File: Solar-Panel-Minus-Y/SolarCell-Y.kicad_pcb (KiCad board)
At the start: 6 copper layers, 64 x 58 mm, 61 parts, among them IC2 TSL2561, J1 XF2M-1015-1A, J3 BATTERY CONNECTOR, J4 B2B-PH-SM4-TB_LF__SN_, U2 Value, U3 SW_SPDT, U4 SW_SPDT

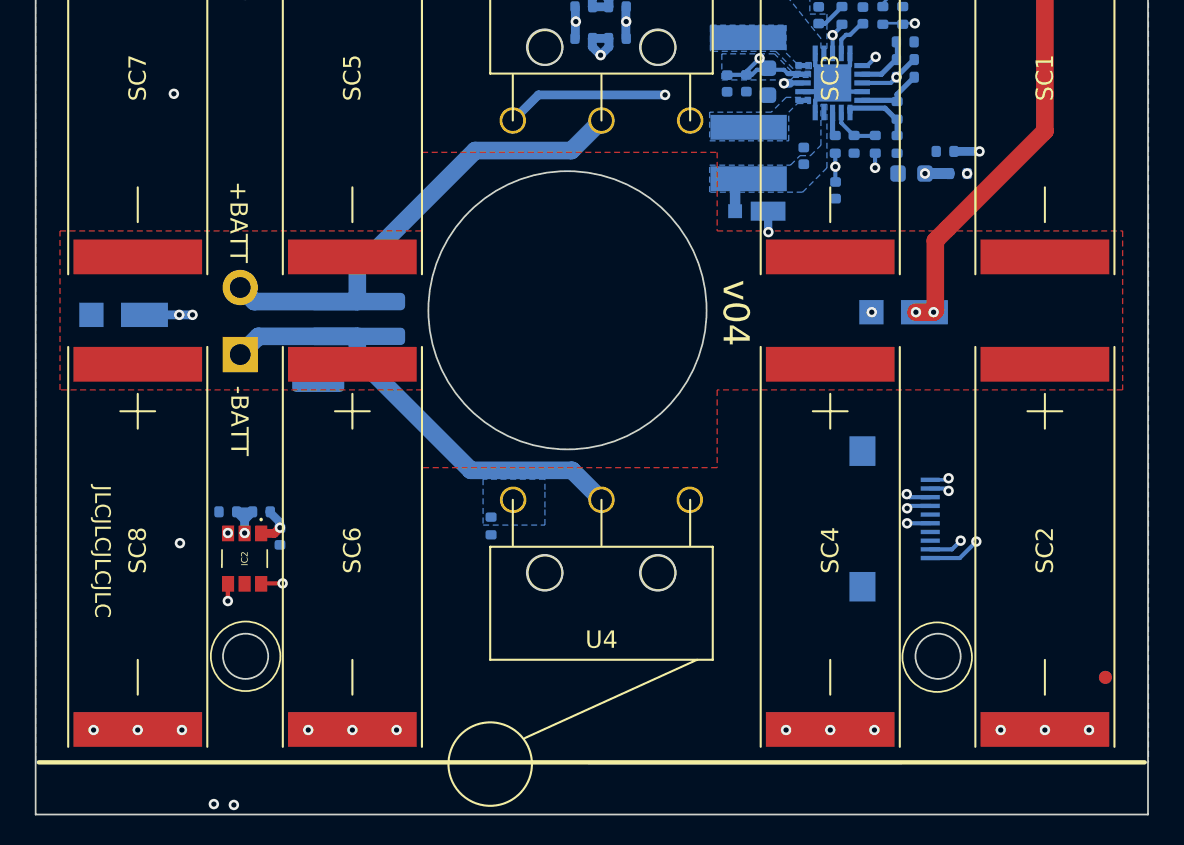
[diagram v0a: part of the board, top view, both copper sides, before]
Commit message: Added missing caps and fixed manufacturing error
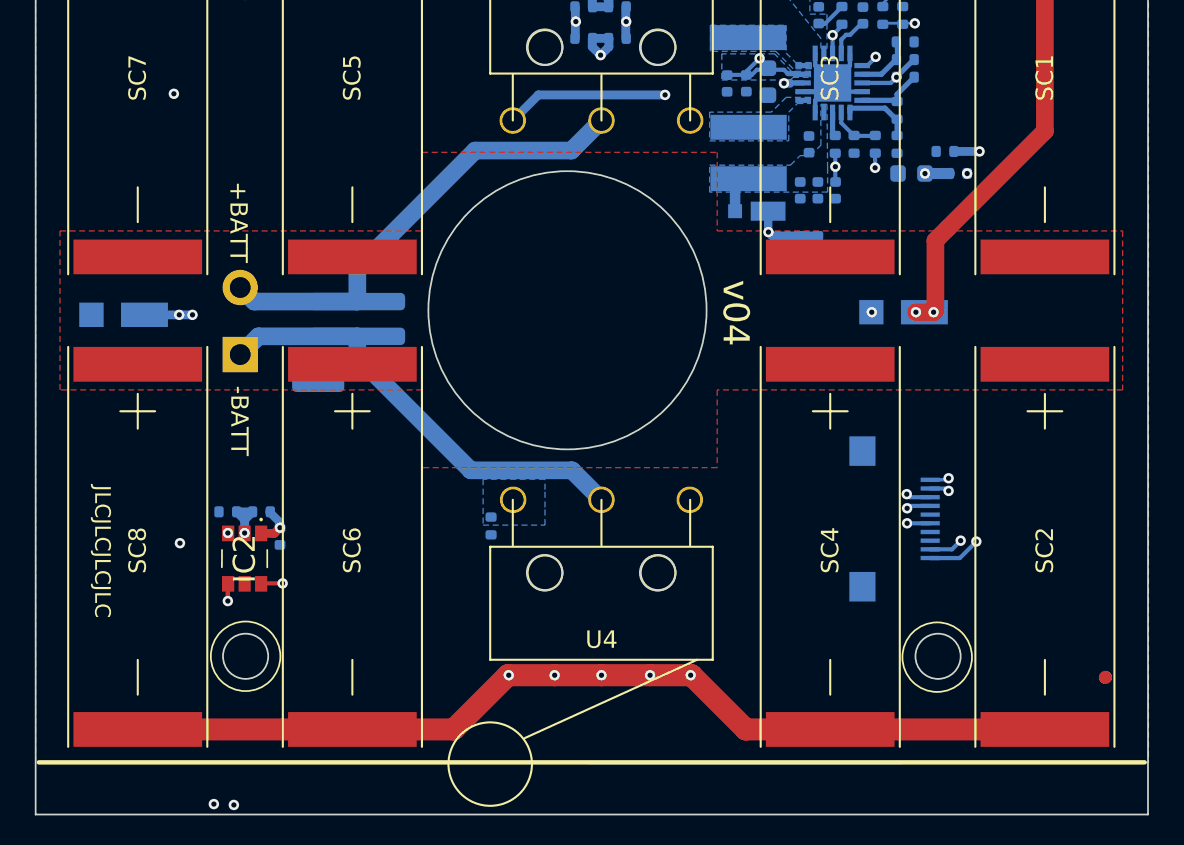
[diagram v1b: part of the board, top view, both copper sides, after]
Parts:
- added C11: 0.1uF, Capacitor_SMD:C_0402_1005Metric, B.Cu at (158.0, 92.1)
- added C12: 100uF, Capacitor_SMD:C_0402_1005Metric, B.Cu at (157.0, 92.1)
- added C13: 0.1uF, Capacitor_SMD:C_0402_1005Metric, B.Cu at (157.0, 95.2)
- added C14: 100uF, Capacitor_SMD:C_0402_1005Metric, B.Cu at (158.0, 95.2)
- moved C7 0.73 mm to (157.5, 89.5)
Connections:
- SC2 pad 2: /coil -> GND
- SC4 pad 2: /coil -> GND
- SC6 pad 2: /coil -> GND
- SC8 pad 2: /coil -> GND
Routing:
- net GND: track 9.43 -> 64.2 mm, vias 1 -> 6
- net +3V3: track 84.8 -> 87.7 mm
- net /coil: vias 18 -> 6

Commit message: More Cleanup
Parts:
- added Ref**: Val**, custom-footprints:ypanel, F.Cu at (164.6, 125.5)
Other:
- board text added: "Cable Pinout 1.BATT_P 2.BATT_N 3.SDA 4.SCL 5.BURN 6.3V3 7.GND 8.GND 9.COIL_N 10.COIL_P"
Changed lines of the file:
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@@
     (property "Sheetname" "")
     (attr smd)
-    (fp_text reference "IC2" (at 0 0.002 -90) (layer "F.SilkS")
-      (effects (font (size 1.27 1.27) (thickness 0.254)))
+    (fp_text reference "IC2" (at 0 0.002007 -90) (layer "F.SilkS")
+      (effects (font (size 0.381 0.381) (thickness 0.0762)))
     )
     (fp_text value "TSL2561" (at 0 0.002 -90) (layer "F.SilkS") hide
@@
       (net 1 "Net-(D11-Pad2)") (pinfunction "V-") (pintype "bidirectional"))
   )
+  (footprint "custom-footprints:ypanel" (layer "F.Cu")
+    (at 164.621794 125.5395)
+    (attr through_hole)
+    (fp_text reference "Ref**" (at 0 0) (layer "F.SilkS") hide
+      (effects (font (size 1.27 1.27) (thickness 0.15)))
+    )
+    (fp_text value "Val**" (at 0 0) (layer "F.SilkS") hide
+      (effects (font (size 1.27 1.27) (thickness 0.15)))
+    )
+    (fp_rect (start -19.4 -0.25) (end -22.5 -0.95) (layer "F.SilkS") (width 0.12) (fill solid))
+    (fp_poly (pts
+        (xy -18.05305 -3.377964)
+        (xy -17.53235 -2.444944)
+        (xy -17.453161 -2.303177)
+        (xy -17.377487 -2.16796)
+        (xy -17.306246 -2.040913)
+        (xy -17.240353 -1.923656)
+        (xy -17.180722 -1.817811)
+        (xy -17.128268 -1.724997)
+        (xy -17.083908 -1.646836)
+        (xy -17.048557 -1.584947)
+        (xy -17.023129 -1.540951)
+        (xy -17.008541 -1.51647)
+        (xy -17.0053 -1.511788)
+        (xy -16.998442 -1.522677)
+        (xy -16.980444 -1.55429)
+        (xy -16.952203 -1.604988)
+        (xy -16.914615 -1.673127)
+        (xy -16.868579 -1.757067)
+        (xy -16.814992 -1.855166)
+        (xy -16.754751 -1.965783)
+        (xy -16.688753 -2.087277)
+        (xy -16.617896 -2.218006)
+        (xy -16.543076 -2.356328)
+        (xy -16.496943 -2.441752)
+        (xy -15.994935 -3.37185)
+        (xy -15.293618 -3.375133)
+        (xy -15.162801 -3.37564)
+        (xy -15.039916 -3.375914)
+        (xy -14.927251 -3.375962)
+        (xy -14.827095 -3.375793)
+        (xy -14.741735 -3.375417)
+        (xy -14.673459 -3.374842)
+        (xy -14.624556 -3.374076)
+        (xy -14.597313 -3.37313)
+        (xy -14.5923 -3.372439)
+        (xy -14.598728 -3.361044)
+        (xy -14.617511 -3.329138)
+        (xy -14.647903 -3.277968)
+        (xy -14.689156 -3.208783)
+        (xy -14.740522 -3.122829)
+        (xy -14.801253 -3.021355)
+        (xy -14.870602 -2.905608)
+        (xy -14.947821 -2.776835)
+        (xy -15.032161 -2.636285)
+        (xy -15.122876 -2.485205)
+        (xy -15.219218 -2.324843)
+        (xy -15.320438 -2.156445)
+        (xy -15.42579 -1.981261)
+        (xy -15.494 -1.867882)
+        (xy -16.3957 -0.369301)
+        (xy -16.3957 1.524)
+        (xy -17.6657 1.524)
+        (xy -17.665956 -0.31115)
+        (xy -19.505676 -3.3782)
+        (xy -18.05305 -3.377964)
+      ) (layer "F.SilkS") (width 0.01) (fill solid))
+  )
   (footprint "SolarCellParts:D2F-L2-2" (layer "F.Cu")
     (at 145.542 88.0872)
@@
     (property "Sheetname" "")
     (attr smd)
-    (fp_text reference "J1" (at -0.37186 -2.68404 270) (layer "B.SilkS")
-      (effects (font (size 1.27 1.27) (thickness 0.254)) (justify mirror))
+    (fp_text reference "J1" (at 0.002007 -2.702789 270) (layer "B.SilkS")
+      (effects (font (size 0.381 0.381) (thickness 0.0762)) (justify mirror))
     )
     (fp_text value "XF2M-1015-1A" (at -0.37186 -2.68404 270) (layer "B.SilkS") hide
@@
   (gr_line (start 146.31035 82.4992) (end 145.99285 82.4992) (layer "B.SilkS") (width 0.12))
   (gr_line (start 113.1824 72.9996) (end 176.784 72.9996) (layer "B.SilkS") (width 0.254))
-  (gr_line (start 113.1824 125) (end 176.784 125) (layer "B.SilkS") (width 0.254))
+  (gr_line (start 113.1824 125.0188) (end 136.3472 125.0188) (layer "B.SilkS") (width 0.254))
+  (gr_line (start 153.6192 125.0188) (end 176.784 125.0188) (layer "B.SilkS") (width 0.254))
   (gr_arc (start 148.811249 117.046117) (mid 147.387097 117.847549) (end 145.76852 117.62236) (layer "B.SilkS") (width 0.12))
   (gr_arc (start 145.707578 117.140822) (mid 146.845333 116.354778) (end 148.011919 117.09736) (layer "B.SilkS") (width 0.12))
@@
   (gr_circle (center 164.9 79.1) (end 166.9 79.1) (layer "F.SilkS") (width 0.1) (fill none))
   (gr_circle (center 125.05 79.1) (end 127.05 79.1) (layer "F.SilkS") (width 0.12) (fill none))
-  (gr_line (start 113.1824 125) (end 176.784 125) (layer "F.SilkS") (width 0.254))
+  (gr_line (start 153.6192 125.0188) (end 176.784 125.0188) (layer "F.SilkS") (width 0.254))
+  (gr_line (start 113.1824 125.0188) (end 136.3472 125.0188) (layer "F.SilkS") (width 0.254))
   (gr_circle (center 125.075 118.9) (end 127.075 118.9) (layer "F.SilkS") (width 0.1) (fill none))
-  (gr_line (start 144.8 125.05) (end 162.8 125.05) (layer "F.SilkS") (width 0.12))
   (gr_line (start 121.6 122.4) (end 121.6 75.6) (layer "Dwgs.User") (width 0.15))
   (gr_line (start 121.6 75.6) (end 121.6 82.6) (layer "Dwgs.User") (width 0.15))
@@
   (gr_line (start 176.975 70) (end 113 70) (layer "Edge.Cuts") (width 0.1))
   (gr_circle (center 142.277236 114.0968) (end 141.247672 114.0968) (layer "Edge.Cuts") (width 0.1) (fill none))
+  (gr_text "v04" (at 151.5364 126.238) (layer "F.Cu")
+    (effects (font (size 1.5 1.5) (thickness 0.3)))
+  )
   (gr_text "+BATT" (at 134.8232 94.8436 90) (layer "B.SilkS")
     (effects (font (size 1 1) (thickness 0.15)) (justify mirror))
@@
     (effects (font (size 0.381 0.381) (thickness 0.0762)) (justify mirror))
   )
-  (gr_text "1" (at 158.115 106.6165 90) (layer "B.SilkS")
+  (gr_text "1" (at 160.528 105.5624 90) (layer "B.SilkS")
     (effects (font (size 1 1) (thickness 0.1778)) (justify mirror))
   )
@@
     (effects (font (size 1 1) (thickness 0.15)) (justify mirror))
   )
+  (gr_text "Cable Pinout\n1.BATT_P\n2.BATT_N\n3.SDA\n4.SCL\n5.BURN\n6.3V3\n7.GND\n8.GND\n9.COIL_N\n10.COIL_P" (at 158.5468 115.1128) (layer "B.SilkS")
+    (effects (font (size 1 1) (thickness 0.15)) (justify left mirror))
+  )
   (gr_text "+BATT" (at 124.6632 93.9292 270) (layer "F.SilkS")
     (effects (font (size 1 1) (thickness 0.15)))
@@
     (effects (font (size 1 1) (thickness 0.15)))
   )
-  (gr_text "v04" (at 153.2636 99.1616 270) (layer "F.SilkS")
-    (effects (font (size 1.5 1.5) (thickness 0.3)))
-  )
   (gr_text "JLCJLCJLCJLC" (at 116.84 112.8776 270) (layer "F.SilkS")
     (effects (font (size 0.9 0.9) (thickness 0.15)))
   )
+  (gr_text "v04" (at 151.5364 126.238) (layer "F.Mask")
+    (effects (font (size 1.5 1.5) (thickness 0.3)))
+  )
   (segment (start 169.60342 95.89008) (end 169.545 95.9485) (width 1) (layer "F.Cu") (net 1))

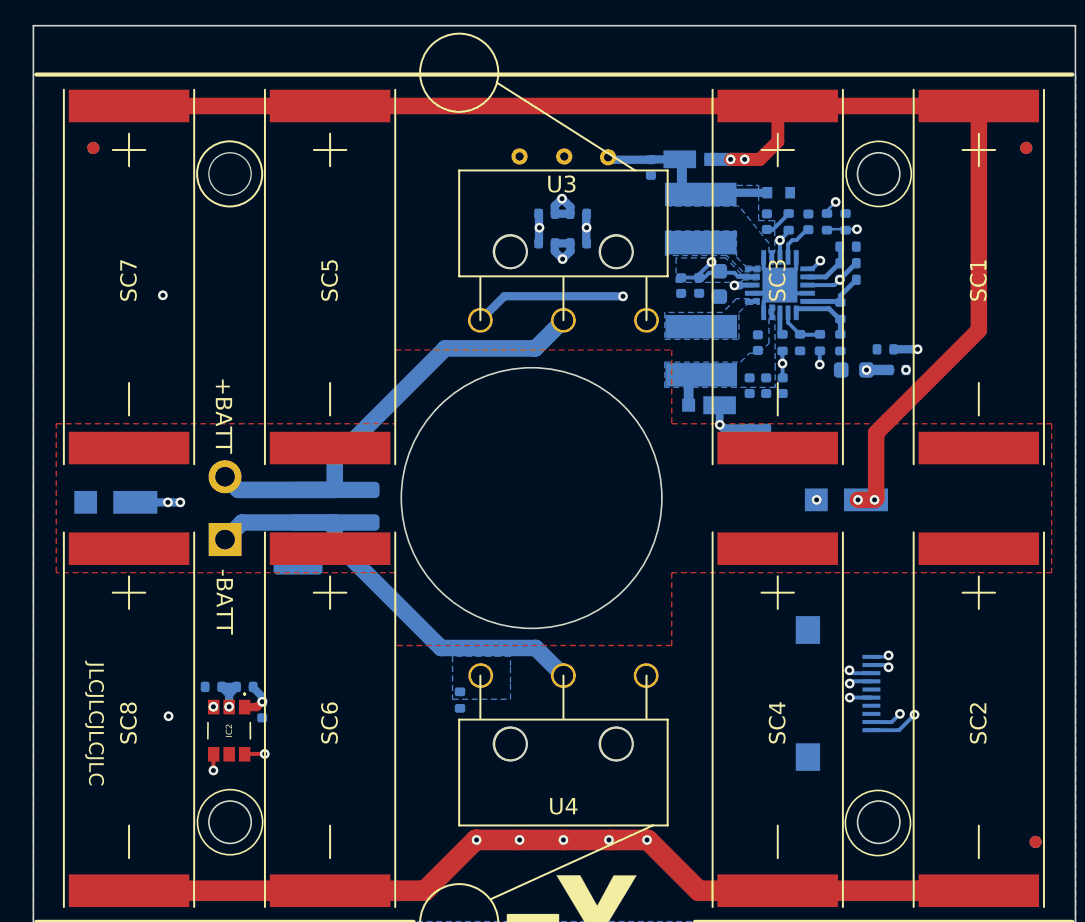
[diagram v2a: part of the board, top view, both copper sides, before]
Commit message: Moved board connectors to North board edges
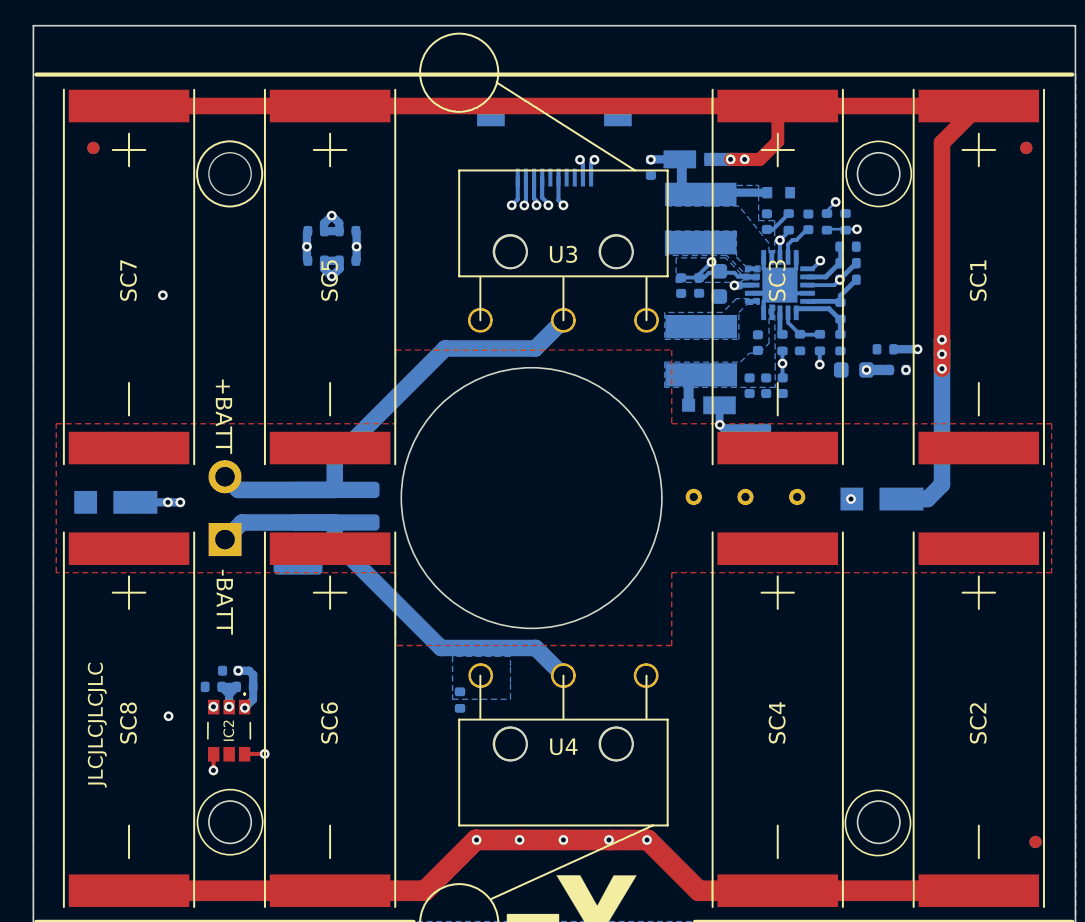
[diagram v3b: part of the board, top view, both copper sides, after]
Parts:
- added Ref**: Val**, custom-footprints:pycubed_mini_logo, B.Cu at (170.8, 107.2)
- moved J1 37.2 mm to (145.0, 79.3), turned to 0 degrees
- moved TP3 23.9 mm to (159.9, 98.9)
- moved TP2 23.7 mm to (156.7, 98.9)
- moved TP1 23.5 mm to (153.5, 98.9)
- moved R10 14.2 mm to (132.3, 84.4)
- moved R16 14.2 mm to (130.4, 82.6)
- moved R19 14.2 mm to (132.3, 82.6)
- moved R9 14.2 mm to (130.4, 84.4)
- moved C5 3.11 mm to (125.1, 109.6), turned to 0 degrees
- moved D11 2.18 mm to (165.1, 99.1)
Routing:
- net COIL_P: track 59.7 -> 23.6 mm
- net COIL_N: track 56.3 -> 21.9 mm
- net /coil: track 16730.3 -> 16699.4 mm
- net VSOLAR: track 12.1 -> 34.7 mm, vias 0 -> 1
- net +3V3: track 87.7 -> 71.6 mm, vias 3 -> 4
- net SCL1: track 43.7 -> 54.0 mm
- net SDA1: track 40.7 -> 49.6 mm
- net BATT_P: track 49.2 -> 40.5 mm, vias 3 -> 2
- net BATT_N: track 23.3 -> 31.5 mm
- net /VSOLAR_FULL: track 87.6 -> 88.6 mm, vias 4 -> 5
